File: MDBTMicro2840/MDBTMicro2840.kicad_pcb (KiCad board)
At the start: 2 copper layers, 4 parts, among them J1 Conn_01x04, J2 USB_C_Receptacle_USB2.0, U1 MDBT50Q-x1MV2, U2 ProMicro

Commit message: Update sch
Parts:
- added C1: 12pF, Capacitor_SMD:C_0201_0603Metric, F.Cu at (142.2, 81.3)
- added C2: 12pF, Capacitor_SMD:C_0201_0603Metric, F.Cu at (137.7, 81.1)
- added C3: 10uF, Capacitor_SMD:C_0201_0603Metric, F.Cu at (135.6, 95.0)
- added C4: 10uF, Capacitor_SMD:C_0201_0603Metric, F.Cu at (137.2, 95.0)
- added D1: 1N5819, Diode_SMD:D_0201_0603Metric, F.Cu at (134.6, 94.0)
- added LD1: RED, LED_SMD:LED_0201_0603Metric, F.Cu at (135.0, 89.9)
- added LD2: BLUE, LED_SMD:LED_0201_0603Metric, F.Cu at (136.3, 99.6)
- added R1: 1k, Resistor_SMD:R_0201_0603Metric, F.Cu at (136.5, 89.9)
- added R2: Rprog, Resistor_SMD:R_0201_0603Metric, F.Cu at (138.0, 89.9)
- added R3: 820k, Resistor_SMD:R_0201_0603Metric, F.Cu at (136.5, 94.0)
- added R4: 2M, Resistor_SMD:R_0201_0603Metric, F.Cu at (138.0, 94.0)
- added R5: 1k, Resistor_SMD:R_0201_0603Metric, F.Cu at (134.8, 99.6)
- added R6: 5.1k, Resistor_SMD:R_0201_0603Metric, F.Cu at (133.6, 92.5)
- added R7: 5.1k, Resistor_SMD:R_0201_0603Metric, F.Cu at (133.6, 95.8)
- added U2: ProMicro, MDBTMicro_library:ProMicro, F.Cu at (127.0, 101.6)
- added U3: XC6220B331MR-G, MDBTMicro_library:SOT-25-5, F.Cu at (136.1, 97.0)
- added U4: TP4057, Package_TO_SOT_SMD:SOT-23-6, F.Cu at (136.1, 91.9)
- added Y1: 32.768kHz, Crystal:Crystal_SMD_3215-2Pin_3.2x1.5mm, F.Cu at (145.8, 81.8)
- J1: value Conn_01x04 -> SWD
- J2: footprint Connector_USB:USB_C_Receptacle_Palconn_UTC16-G -> Connector_USB:USB_C_Receptacle_HRO_TYPE-C-31-M-12
- U1: footprint MDBTMicro_library:MDBT50Q -> RF_Module:Raytac_MDBT50Q
- moved J1 21.3 mm to (168.7, 89.7)
- moved U1 3.54 mm to (151.6, 94.0)
- moved J2 0.89 mm to (128.0, 94.0)
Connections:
- net /RESET renamed RESET
- net /SWDCLK renamed SWCLK
- net /SWDIO renamed SWDIO
- net /USB_D+ renamed USB_D+
- net /USB_D- renamed USB_D-
- net /VBUS renamed VBUS
- J1 pad 1: VDD -> nRF_VDD
- J2 pad A5: unconnected-(J2-PadA5) -> Net-(J2-PadA5)
- J2 pad B5: unconnected-(J2-PadB5) -> Net-(J2-PadB5)
- J2 pad S1: GND -> unconnected-(J2-PadS1)
- U1 pad 15: unconnected-(U1-Pad15) -> GND
- U1 pad 17: unconnected-(U1-Pad17) -> Net-(U1-Pad17)
- U1 pad 18: unconnected-(U1-Pad18) -> Net-(U1-Pad18)
- U1 pad 20: unconnected-(U1-Pad20) -> BATTERT_PIN
- U1 pad 28: VDD -> nRF_VDD
- U1 pad 3: unconnected-(U1-Pad3) -> LED_PIN
- U1 pad 30: unconnected-(U1-Pad30) -> nRF_VDD
- U1 pad 33: unconnected-(U1-Pad33) -> GND
- U1 pad 55: unconnected-(U1-Pad55) -> GND
- U2 pad 13: unconnected-(U2-Pad13) -> VBAT
- U2 pad 14: unconnected-(U2-Pad14) -> GND
- U2 pad 16: unconnected-(U2-Pad16) -> nRF_VDD
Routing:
- net RESET: track 21.5 -> 0.00 mm, vias 1 -> 0
- net /P0.06: track 19.7 -> 0.00 mm
- net /P0.08: track 16.8 -> 0.00 mm
- net GND: track 14.7 -> 0.00 mm
- net /P1.06: track 13.0 -> 0.00 mm, vias 1 -> 0
- net /P0.28: track 12.3 -> 0.00 mm, vias 1 -> 0
- net /P0.02: track 11.0 -> 0.00 mm, vias 1 -> 0
- net /P0.15: track 8.63 -> 0.00 mm
- net /P0.30: track 8.42 -> 0.00 mm
- net /P1.11: track 7.82 -> 0.00 mm
- net /P0.03: track 7.74 -> 0.00 mm, vias 1 -> 0
- net /P0.17: track 7.20 -> 0.00 mm
- net /P0.31: track 7.00 -> 0.00 mm
- net /P0.20: track 5.95 -> 0.00 mm
- net /P0.29: track 5.26 -> 0.00 mm
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
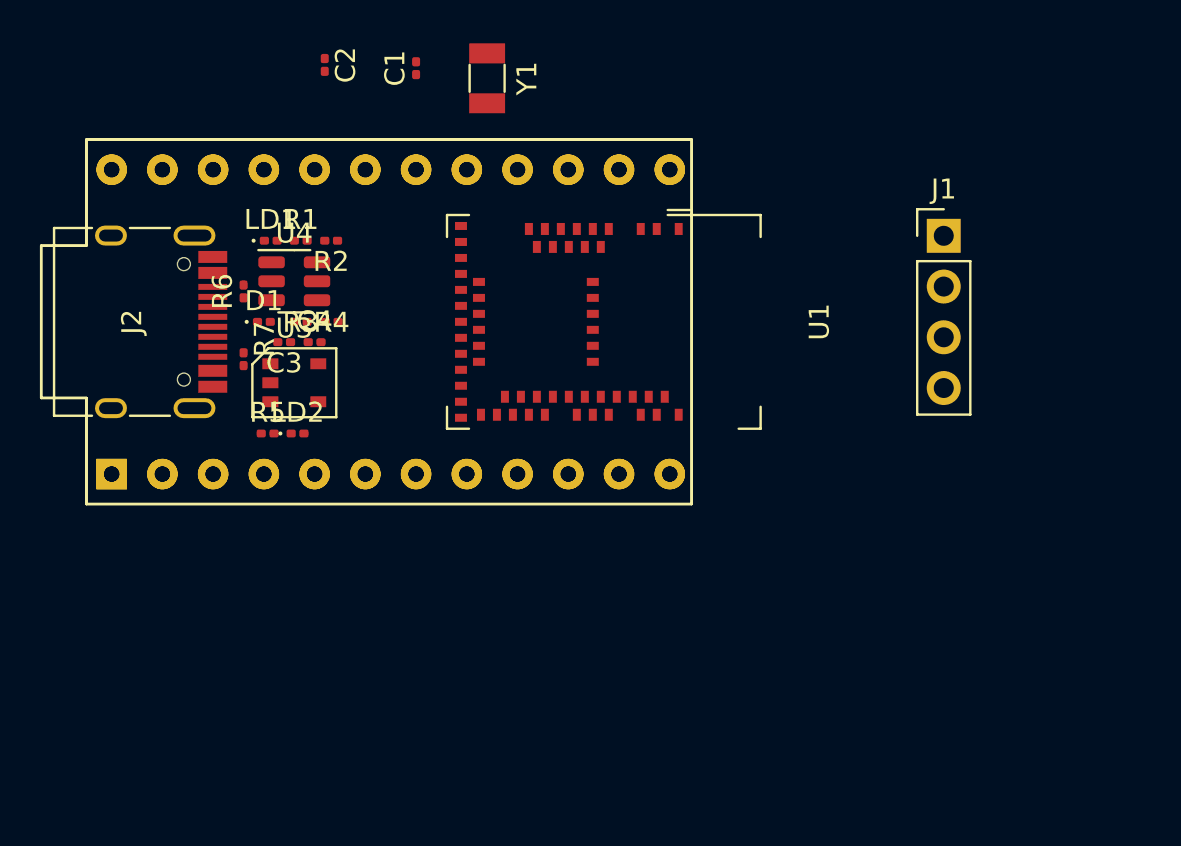
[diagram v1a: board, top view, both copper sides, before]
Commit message: Update USB footprint
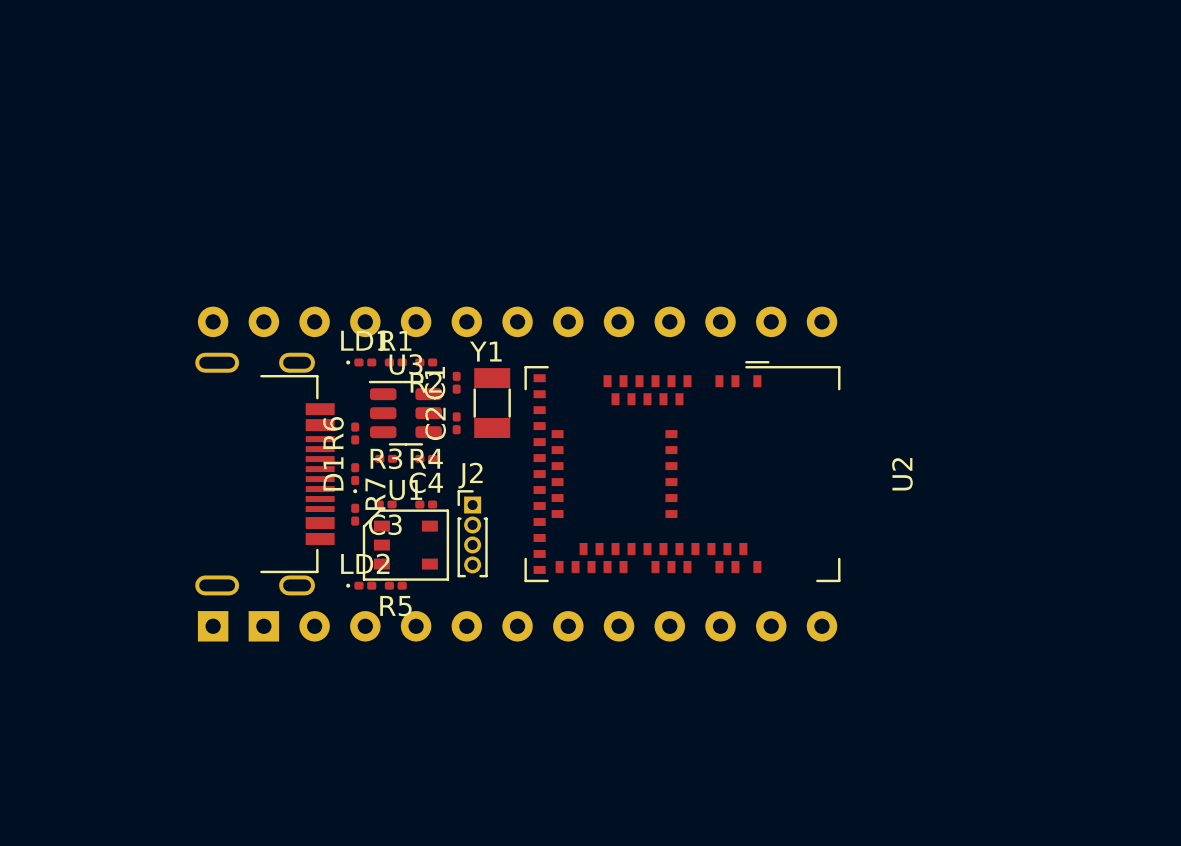
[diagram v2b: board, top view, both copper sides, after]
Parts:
- removed the U2 at (127.0, 101.6) (x2)
- added ?: , , F.Cu at (132.1, 109.2)
- added ?: , , F.Cu at (132.1, 94.0)
- added U4: ProMicro, MDBTMicro_library:ProMicro, F.Cu at (134.6, 109.2)
- J1: renamed from J2; footprint Connector_USB:USB_C_Receptacle_HRO_TYPE-C-31-M-12 -> MDBTMicro_library:USB Type-C Mid-Mount Receptacle 16P
- J2: renamed from J1; footprint Connector_PinHeader_2.54mm:PinHeader_1x04_P2.54mm_Vertical -> Connector_PinHeader_1.00mm:PinHeader_1x04_P1.00mm_Vertical
- moved J2 27.2 mm to (145.1, 103.1)
- moved C2 19.1 mm to (144.3, 99.1)
- moved Y1 16.3 mm to (146.1, 98.0)
- moved C1 15.9 mm to (144.3, 97.0)
- moved R5 9.96 mm to (141.2, 107.2), turned to 180 degrees
- moved C4 9.86 mm to (142.7, 103.1)
- moved U1 9.86 mm to (141.7, 105.2)
- moved C3 9.58 mm to (140.7, 103.1)
- moved R7 9.58 mm to (139.2, 103.6)
- moved J1 9.16 mm to (133.1, 101.6)
- moved R6 9.04 mm to (139.2, 99.6)
- moved D1 8.89 mm to (139.2, 101.6), turned to 90 degrees
- moved U3 8.65 mm to (141.7, 98.6)
- moved U2 8.58 mm to (155.6, 101.6)
- moved LD2 8.34 mm to (139.7, 107.2)
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- renumbered U3 to U1, U1 to U2, U4 to U3
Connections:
- J1 pad S1: unconnected-(J2-PadS1) -> GND

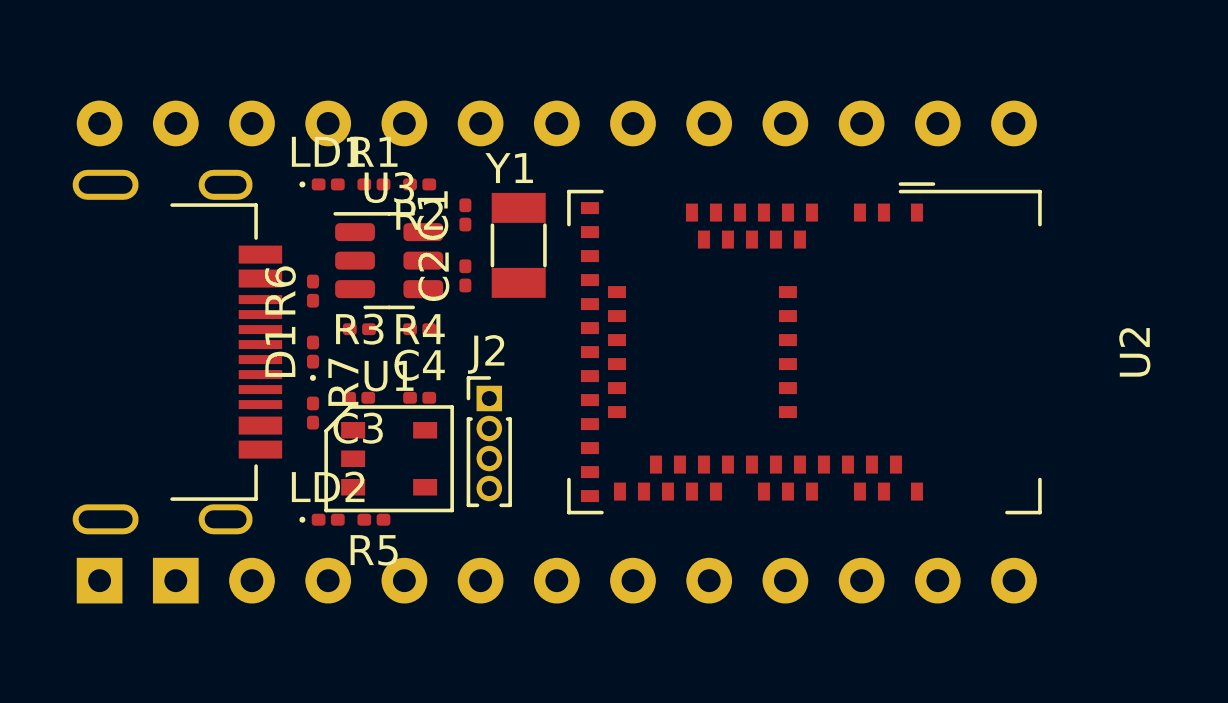
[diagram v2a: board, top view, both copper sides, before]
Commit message: Update to pass the DRC
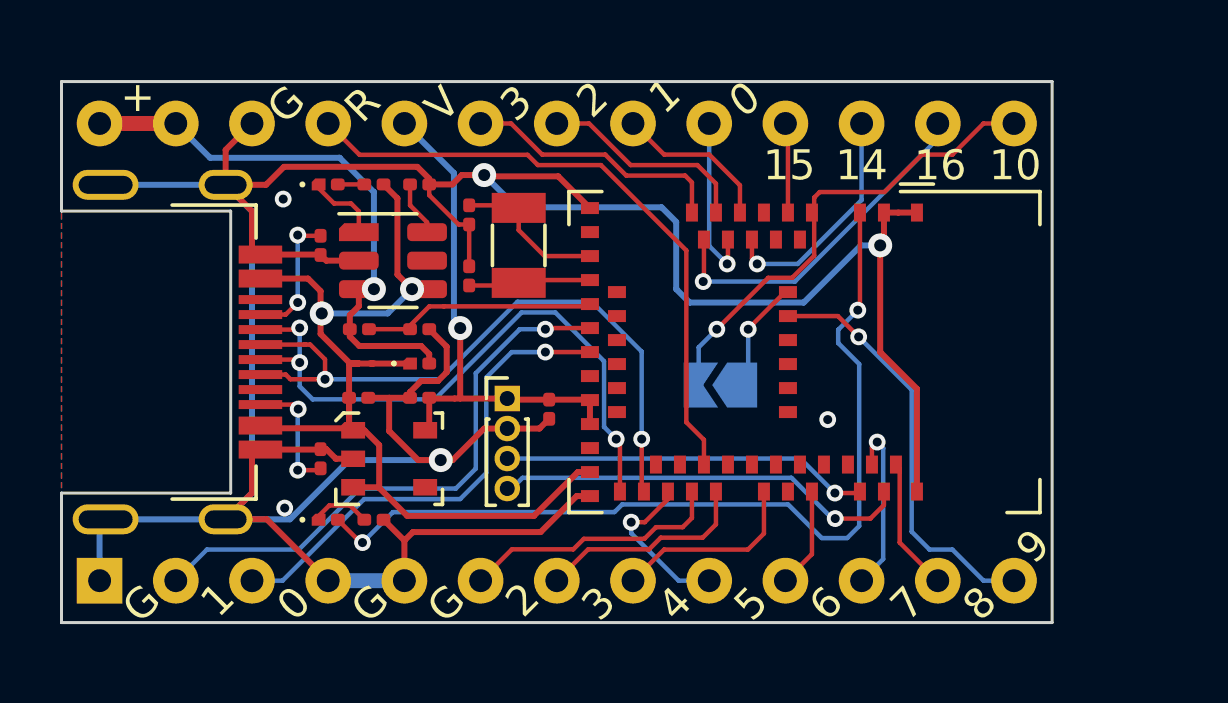
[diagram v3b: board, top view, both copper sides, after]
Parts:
- added C3: 10uF, Capacitor_SMD:C_0201_0603Metric, F.Cu at (147.1, 103.5)
- added JP1: SolderJumper_2_Open, Jumper:SolderJumper-2_P1.3mm_Open_TrianglePad1.0x1.5mm, B.Cu at (152.8, 102.7)
- moved D1 3.58 mm to (142.7, 102.0), turned to 0 degrees
- moved R6 1.55 mm to (139.4, 98.0), turned to -90 degrees
- moved R7 1.55 mm to (139.4, 105.2), turned to 90 degrees
- moved J2 0.60 mm to (145.7, 103.1)
- moved C1 0.13 mm to (144.4, 97.0)
- moved C2 0.13 mm to (144.4, 99.1)
- moved U3 0.13 mm to (141.9, 98.6)
- renumbered C3 to C4, C4 to C5, Y1 to X1
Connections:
- net BATTERT_PIN renamed BATTERY_PIN
- U2 pad 56: unconnected-(U2-Pad56) -> /P1.04
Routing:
- net GND: track 0.00 -> 118.0 mm, vias 0 -> 6
- net VBUS: track 0.00 -> 33.4 mm, vias 0 -> 2
- net LED_PIN: track 0.00 -> 29.9 mm, vias 0 -> 2
- net USB_D+: track 0.00 -> 22.9 mm, vias 0 -> 2
- net USB_D-: track 0.00 -> 22.0 mm, vias 0 -> 3
- net RESET: track 0.00 -> 21.1 mm
- net /P0.06: track 0.00 -> 19.2 mm, vias 0 -> 1
- net VBAT: track 0.00 -> 18.7 mm, vias 0 -> 1
- net nRF_VDD: track 0.00 -> 17.3 mm, vias 0 -> 1
- net /P0.08: track 0.00 -> 16.3 mm, vias 0 -> 1
- net /P1.11: track 0.00 -> 16.1 mm, vias 0 -> 1
- net /P1.06: track 0.00 -> 14.0 mm, vias 0 -> 1
- net SWCLK: track 0.00 -> 13.9 mm, vias 0 -> 1
- net SWDIO: track 0.00 -> 12.3 mm, vias 0 -> 1
- net /P0.28: track 0.00 -> 11.7 mm, vias 0 -> 1
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- added copper zone on B.Cu, net GND
- added copper zone on F.Cu, net GND
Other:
- board outline added: 33 x 18 mm
- board text added: "+"
- board text added: "0"
- board text added: "0.02"
- board text added: "0.03"
- board text added: "0.09"
- board text added: "0.10"
- board text added: "0.13"
- board text added: "0.15"
- board text added: "0.17"
- board text added: "0.20"
- board text added: "0.24"
- board text added: "0.28"
- board text added: "0.29"
- board text added: "0.30"
- board text added: "0.31"
- board text added: "1"
- board text added: "1.06"
- board text added: "1.11"
- board text added: "1.13"
- board text added: "10"
- board text added: "14"
- board text added: "15"
- board text added: "16"
- board text added: "2"
- board text added: "3"
- board text added: "4"
- board text added: "5"
- board text added: "6"
- board text added: "7"
- board text added: "8"
- board text added: "9"
- board text added: "G"
- board text added: "GND"
- board text added: "MDBTMicro2840 v1.0"
- board text added: "R"
- board text added: "RST"
- board text added: "Rx"
- board text added: "SWCLK"
- board text added: "SWDIO"
- board text added: "Tx"
- board text added: "V"
- board text added: "VDD"
